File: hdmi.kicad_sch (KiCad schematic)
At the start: 58 parts, among them J13 HDMI-Mini-C_WE_685119136923, Q1 PJE138K, Q12 PJE138K, Q2 PJE138K, Q3 PJE138K, U36 TS3DV642RUARQ1, U43 NTS0102_XSON, U44 TPD4E05U06QDQARQ1, U45 TPD4E05U06QDQARQ1, U46 TPD4E05U06QDQARQ1

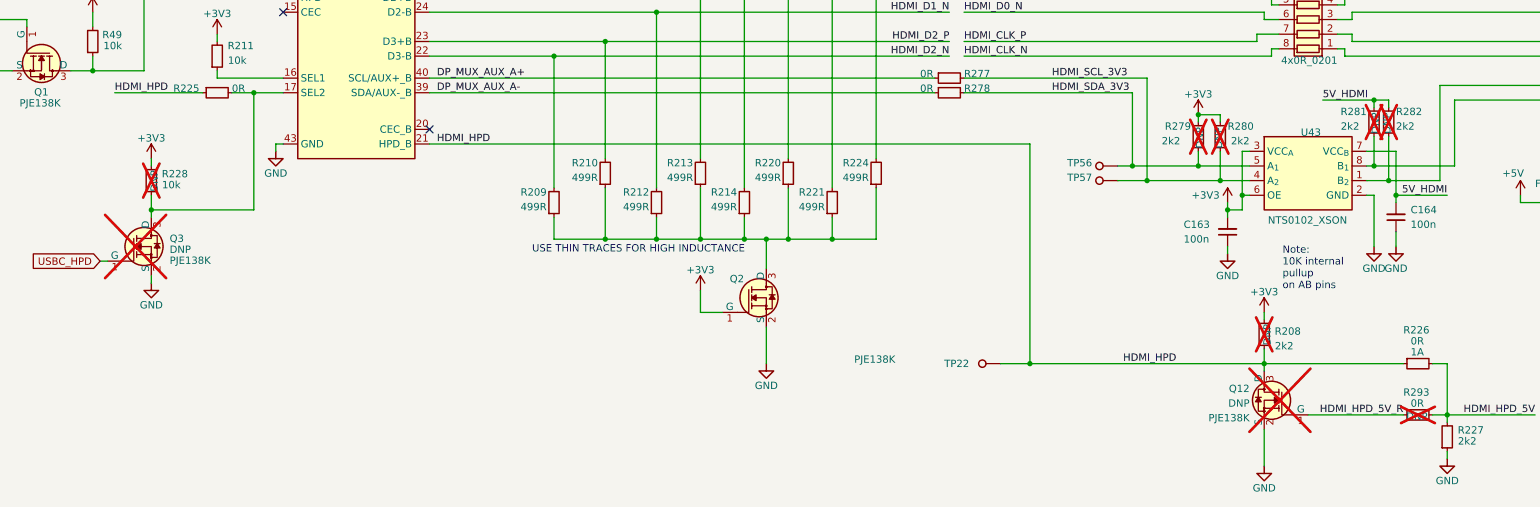
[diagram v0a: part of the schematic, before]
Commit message: 5/16 Commit: Sch Mods added and beginning Development on PCB layout
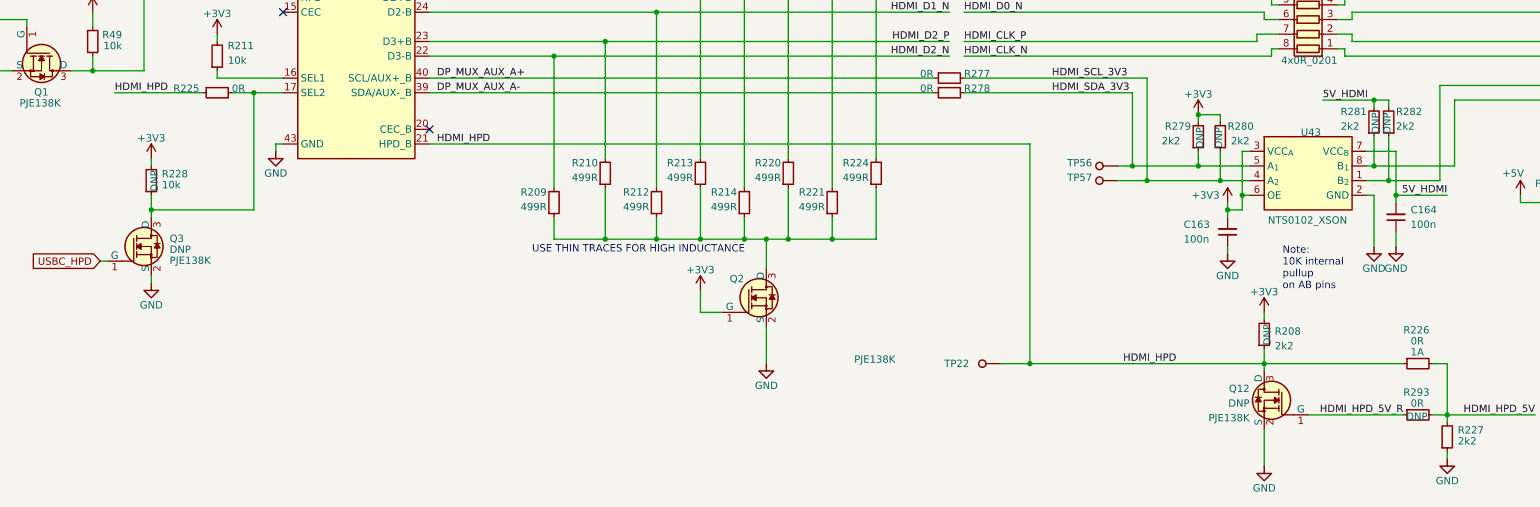
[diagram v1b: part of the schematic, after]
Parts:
- Q12, Q3, R208, R228, R279, R280, R281, R282, R293: now fitted
